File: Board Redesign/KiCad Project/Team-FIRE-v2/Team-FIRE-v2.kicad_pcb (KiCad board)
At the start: 2 copper layers, 95.2 x 88.9 mm, 28 parts, among them J1 Conn_01x11, J2 Screw_Terminal_01x04, U1 ADG732BSUZ

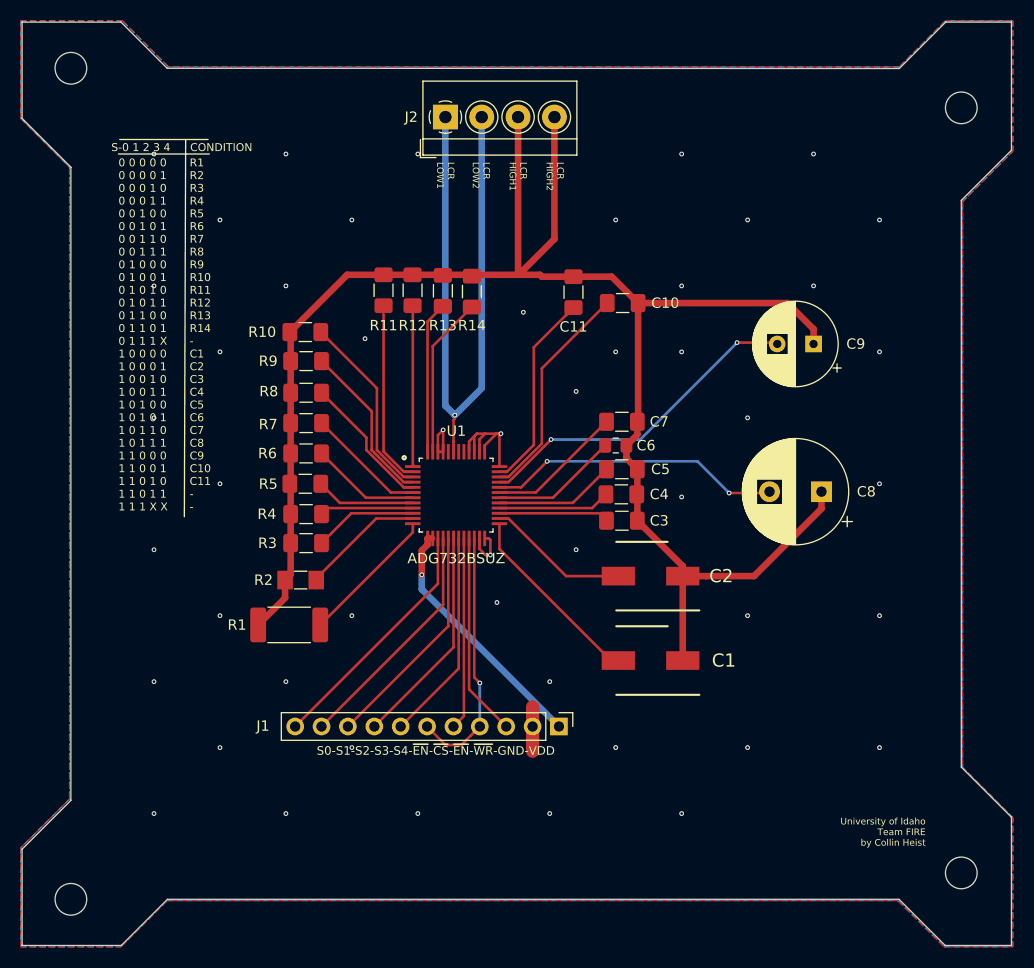
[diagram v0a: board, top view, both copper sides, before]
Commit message: Added SAMD51 Breakout
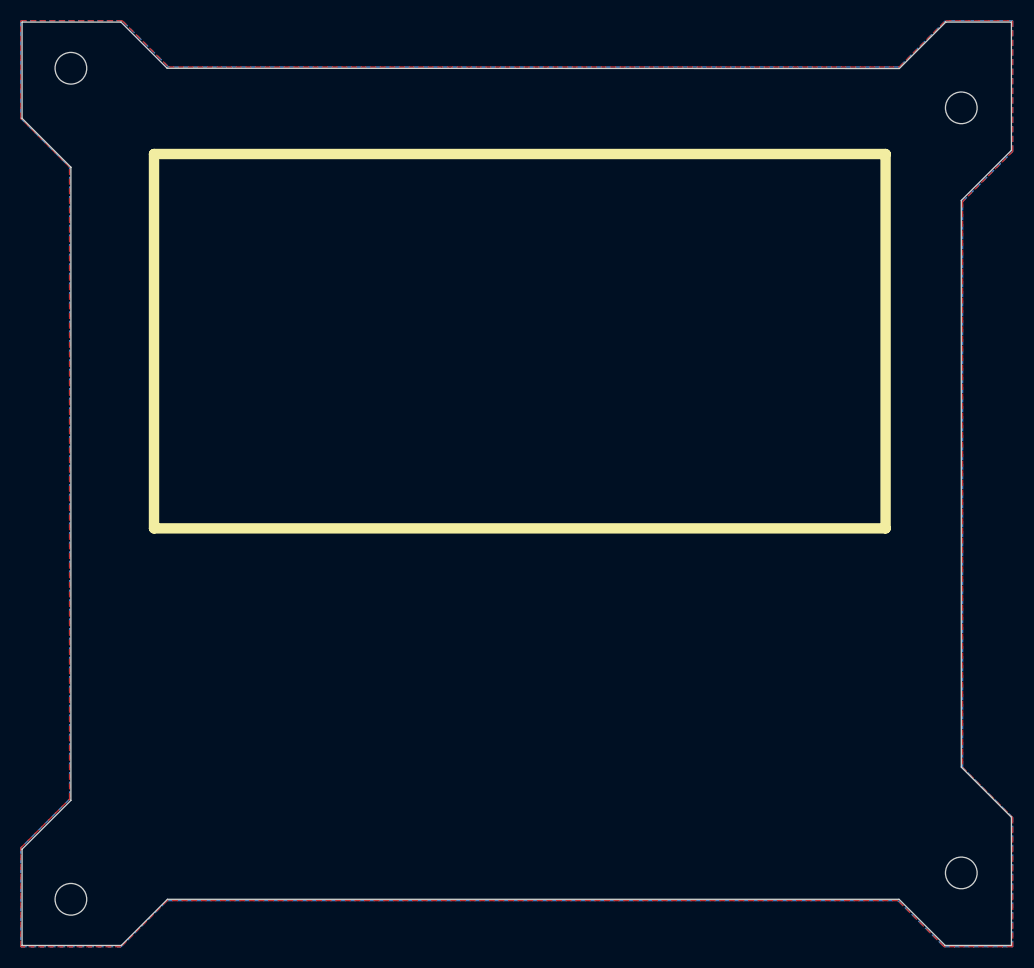
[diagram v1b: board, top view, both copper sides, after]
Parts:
- removed C1, C2: 47u, EEH-ZA1E470V:CAPAE660X640N
- removed C10, C11: 47u, Capacitor_SMD:C_1206_3216Metric_Pad1.42x1.75mm_HandSolder
- removed C3, C4, C5, C7: 0.1u, Capacitor_SMD:C_1206_3216Metric_Pad1.42x1.75mm_HandSolder
- removed C6: 0.1u, Capacitor_SMD:C_0805_2012Metric_Pad1.15x1.40mm_HandSolder
- removed C8: 10, Capacitor_THT:CP_Radial_D10.0mm_P5.00mm
- removed C9: 2.2, Capacitor_THT:CP_Radial_D8.0mm_P3.50mm
- removed J1: Conn_01x11, Connector_PinHeader_2.54mm:PinHeader_1x11_P2.54mm_Vertical
- removed J2: Screw_Terminal_01x04, TerminalBlock_4Ucon:TerminalBlock_4Ucon_1x04_P3.50mm_Horizontal
- removed R1: 1.5k, Resistor_SMD:R_2512_6332Metric_Pad1.52x3.35mm_HandSolder
- removed R10, R11, R12, R13, R14, R9: 10k, Resistor_SMD:R_1206_3216Metric_Pad1.42x1.75mm_HandSolder
- removed R2: 1k, Resistor_SMD:R_MiniMELF_MMA-0204
- removed R3, R4, R5: 1k, Resistor_SMD:R_1206_3216Metric_Pad1.42x1.75mm_HandSolder
- removed R6: 20m, Resistor_SMD:R_1206_3216Metric_Pad1.42x1.75mm_HandSolder
- removed R7: 470m, Resistor_SMD:R_1206_3216Metric_Pad1.42x1.75mm_HandSolder
- removed R8: 100, Resistor_SMD:R_1206_3216Metric_Pad1.42x1.75mm_HandSolder
- removed U1: ADG732BSUZ, ADG732BSUZ:QFP50P900X900X120-49N
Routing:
- net LCR_HIGH1: track 172.5 -> 0.00 mm
- net LCR_LOW1: track 62.4 -> 0.00 mm, vias 1 -> 0
- net Net-(C9-Pad2): track 32.4 -> 0.00 mm, vias 2 -> 0
- net Net-(C8-Pad2): track 28.4 -> 0.00 mm, vias 2 -> 0
- net GND: track 27.6 -> 0.00 mm, vias 49 -> 0
- net ~EN: track 24.9 -> 0.00 mm, vias 1 -> 0
- net VDD: track 24.2 -> 0.00 mm, vias 1 -> 0
- net SELECT0: track 23.8 -> 0.00 mm
- net SELECT1: track 23.0 -> 0.00 mm
- net SELECT2: track 22.1 -> 0.00 mm
- net Net-(C10-Pad2): track 21.5 -> 0.00 mm
- net SELECT3: track 21.3 -> 0.00 mm
- net SELECT4: track 20.4 -> 0.00 mm
- net Net-(C11-Pad2): track 20.3 -> 0.00 mm
- net ~WR: track 19.6 -> 0.00 mm
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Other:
- board text removed: "0 0 0 0 0 0 0 0 0 1 0 0 0 1 0 0 0 0 1 1 0 0 1 0 0 0 0 1 0 1 0 0 1 1 0 0 0 1 1 1 0 1 0 0 0 0 1 0 0 1 0 1 0 1 0 0 1 0 1 1 0 1 1 0 0 0 1 1 0 1 0 1 1 1 X 1 0 0 0 0 1 0 0 0 1 1 0 0 1 0 1 0 0 1 1 1 0 1 0 0 1 0 1 0 1 1 0 1 1 0 1 0 1 1 1 1 1 0 0 0 1 1 0 0 1 1 1 0 1 0 1 1 0 1 1 1 1 1 X X"
- board text removed: "CONDITION"
- board text removed: "LCR HIGH1"
- board text removed: "LCR HIGH2"
- board text removed: "LCR LOW1"
- board text removed: "LCR LOW2"
- board text removed: "R1 R2 R3 R4 R5 R6 R7 R8 R9 R10 R11 R12 R13 R14 - C1 C2 C3 C4 C5 C6 C7 C8 C9 C10 C11 - -"
- board text removed: "S-0 1 2 3 4"
- board text removed: "S0-S1-S2-S3-S4-~EN~-~CS~-~EN~-~WR~-GND-VDD"
- board text removed: "University of Idaho Team FIRE by Collin Heist"

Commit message: Fix connections
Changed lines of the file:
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@@
   (general
     (thickness 1.6)
-    (drawings 29)
+    (drawings 25)
     (tracks 0)
     (zones 0)
@@
     (uvia_drill 0.1016)
   )
-  (gr_line (start 108.5342 38.1) (end 38.1 38.1) (layer F.SilkS) (width 1))
-  (gr_line (start 108.5342 74.1426) (end 108.5342 38.1) (layer F.SilkS) (width 1))
-  (gr_line (start 38.1 74.1426) (end 108.5342 74.1426) (layer F.SilkS) (width 1))
-  (gr_line (start 38.1 38.1) (end 38.1 74.1426) (layer F.SilkS) (width 1))
   (gr_line (start 114.2746 114.3) (end 120.65 114.3) (layer Edge.Cuts) (width 0.0254))
   (gr_line (start 34.9504 114.3) (end 25.4 114.3) (layer Edge.Cuts) (width 0.0254))

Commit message: Finished PMICs
- Finished stuff on schematic page 3!
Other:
- copper layers 2 -> 4
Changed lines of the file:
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@@
   (layers
     (0 F.Cu signal)
+    (1 GND.Cu power)
+    (2 PWR.Cu power)
     (31 B.Cu signal)
     (32 B.Adhes user)
     (33 F.Adhes user)
-    (34 B.Paste user hide)
+    (34 B.Paste user)
     (35 F.Paste user)
-    (36 B.SilkS user hide)
+    (36 B.SilkS user)
     (37 F.SilkS user)
     (38 B.Mask user)
     (39 F.Mask user)
-    (40 Dwgs.User user hide)
-    (41 Cmts.User user hide)
-    (42 Eco1.User user hide)
-    (43 Eco2.User user hide)
+    (40 Dwgs.User user)
+    (41 Cmts.User user)
+    (42 Eco1.User user)
+    (43 Eco2.User user)
     (44 Edge.Cuts user)
-    (45 Margin user hide)
-    (46 B.CrtYd user hide)
-    (47 F.CrtYd user hide)
+    (45 Margin user)
+    (46 B.CrtYd user)
+    (47 F.CrtYd user)
     (48 B.Fab user)
-    (49 F.Fab user hide)
+    (49 F.Fab user)
   )
   (setup
@@
     (connect_pads (clearance 0.508))
     (min_thickness 0.254)
-    (fill (arc_segments 32) (thermal_gap 0.508) (thermal_bridge_width 0.508))
+    (fill yes (arc_segments 32) (thermal_gap 0.508) (thermal_bridge_width 0.508))
     (polygon
       (pts
@@
     (connect_pads (clearance 0.508))
     (min_thickness 0.254)
-    (fill (arc_segments 32) (thermal_gap 0.508) (thermal_bridge_width 0.508))
+    (fill yes (arc_segments 32) (thermal_gap 0.508) (thermal_bridge_width 0.508))
     (polygon
       (pts
